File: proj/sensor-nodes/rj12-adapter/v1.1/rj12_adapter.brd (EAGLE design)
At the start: 78.7 x 54.6 mm, 67 parts, among them J1 54602-908LF, J3 54602-908LF, J5 OPENAG-I2C-RJ12, J6 OPENAG-I2C-RJ12, U1 R-78E5.0-1.0, U2 PCA9615, U4 LM2937, U5 PCA9615

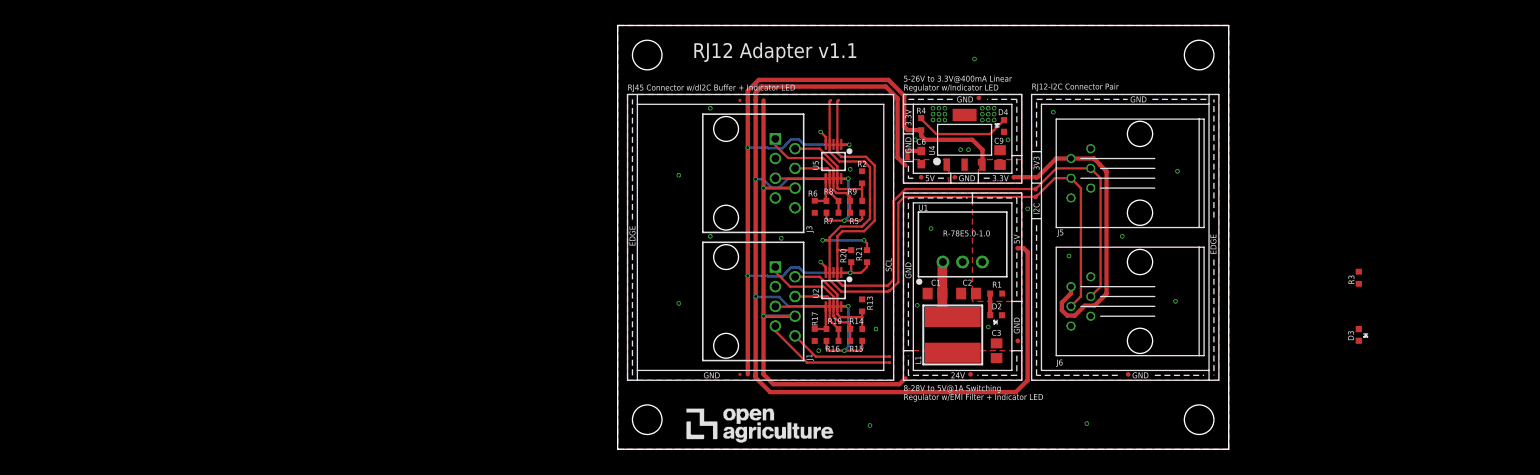
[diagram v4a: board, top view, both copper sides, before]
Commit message: solidifying style and naming conventions
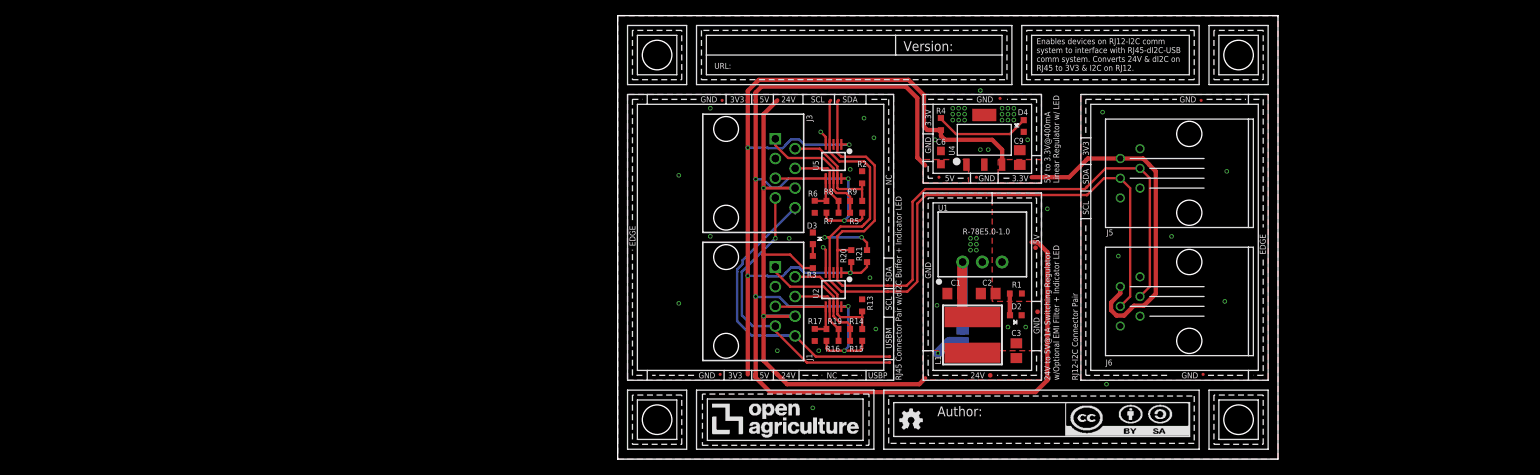
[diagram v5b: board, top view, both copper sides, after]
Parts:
- removed FRAME1: (no value), openag-frames:DOCFIELD
- removed TP12, TP13, TP14: TPTP06R, openag-testpads:TP06R
- added SJ1: (no value), openag-connectors:SOLDERJUMPER_REFLOW_NOPASTE
- added TP27, TP28: TPTP06R, openag-testpads:TP06R
- added TP30: TPTP04R, openag-testpads:TP04R
- added U$6: AUTHOR, openag-frames:AUTHOR
- added U$7: TITLE, openag-frames:TITLE
- TP1, TP10, TP11, TP15, TP2, TP29, TP4, TP6, TP7: value TPTP06R -> TPTP04R; device openag-testpads:TP06R -> openag-testpads:TP04R
- U$5: device openag-frames:OPENAG-LOGO-750-MIL -> openag-frames:LOGO
- U4: value LM2937 -> LM2937-3.3V
- moved D3 71.5 mm to (25.1, 27.2)
- moved R3 70.4 mm to (25.1, 24.1), turned to 270 degrees
- moved TP29 44.3 mm to (75.4, 9.65)
- moved TP1 31.9 mm to (40.1, 41.1), turned to 0 degrees
- moved TP15 23.6 mm to (60.5, 32.8)
- moved TP11 23.5 mm to (75.2, 45.0)
- moved TP2 23.4 mm to (41.4, 35.1), turned to 0 degrees
- moved TP3 16.8 mm to (48.0, 9.53), turned to 0 degrees
- moved TP6 12.3 mm to (53.3, 35.1)
- moved TP4 11.7 mm to (49.3, 45.2)
- moved TP10 10.8 mm to (46.2, 35.1)
- moved TP7 9.60 mm to (60.4, 37.3)
- moved J5 6.35 mm to (73.7, 35.6)
- moved J6 6.35 mm to (73.7, 19.1)
- moved U$3 5.08 mm to (80.0, 3.81)
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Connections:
- removed net IO: J6.2
- net +24V: now also L1.1, SJ1.1, TP3.TP; no longer L1.P$1, TP1.TP
- net +3V3: now also TP1.1, TP6.1, TP7.1; no longer TP10.TP, TP11.TP, TP7.TP
- net +5V: now also TP2.1, TP27.TP; no longer TP29.TP, TP3.TP
- net 24V_EMI: now also L1.2, SJ1.2; no longer L1.P$2
- net GND: now also TP10.1, TP11.1, TP28.TP, TP29.1, TP4.1; no longer TP13.TP, TP15.TP, TP2.TP, TP4.TP, TP6.TP
- net SCL: now also TP15.1; no longer TP12.TP
- net SDA: now also TP30.1; no longer TP14.TP
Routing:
- net USBM: track 13.3 -> 40.0 mm
- net USBP: track 17.1 -> 38.8 mm, vias 0 -> 1
- net +24V: track 66.7 -> 79.9 mm, vias 2 -> 3
- net 24V_EMI: track 7.68 -> 16.4 mm
- net +3V3: track 150.6 -> 157.2 mm
- net SDA: track 95.3 -> 101.6 mm
- net +5V: track 171.6 -> 177.8 mm
- net SCL: track 100.0 -> 105.9 mm
- net N$7: track 0.00 -> 1.52 mm
- net GND: track 6.13 -> 5.28 mm, vias 44 -> 54
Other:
- board size 78.7 x 54.6 mm -> 85.1 x 57.2 mm
- board text added: "24V to 5V@1A Switching Regulator w/Optional EMI Filter + Indicator LED"
- board text added: "5V to 3.3V@400mA Linear Regulator w/ LED"
- board text added: "EMI Bypass"
- board text added: "Enables devices on RJ12-I2C comm system to interface with RJ45-dI2C-USB comm system. Converts 24V & dI2C on RJ45 to 3V3 & I2C on RJ12."
- board text added: "NC"
- board text added: "RJ45 Connector Pair w/dI2C Buffer + Indicator LED"
- board text added: "SDA"
- board text added: "USBM"
- board text added: "USBP"
- board text removed: "5-26V to 3.3V@400mA Linear Regulator w/Indicator LED"
- board text removed: "8-28V to 5V@1A Switching Regulator w/EMI Filter + Indicator LED"
- board text removed: "I2C"
- board text removed: "RJ12 Adapter v1.1"
- board text removed: "RJ45 Connector w/dI2C Buffer + Indicator LED"
